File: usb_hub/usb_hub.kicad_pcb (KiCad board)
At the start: 2 copper layers, 100 x 23 mm, 127 parts, among them P1 CONN_01X02, U1 TPS2044B, U10 USB_A_FEMALE, U11 SN75240, U12 SN75240, U13 USB_A_FEMALE, U14 USB_A_FEMALE, U15 USB_A_FEMALE, U16 USB_A_FEMALE, U2 TPS2044B, U3 TUSB2077A, U4 TPS76333, U5 USB_A_MALE, U6 SN75240, U7 SN75240, U8 USB_A_FEMALE, U9 USB_A_FEMALE, X1 6 MHz

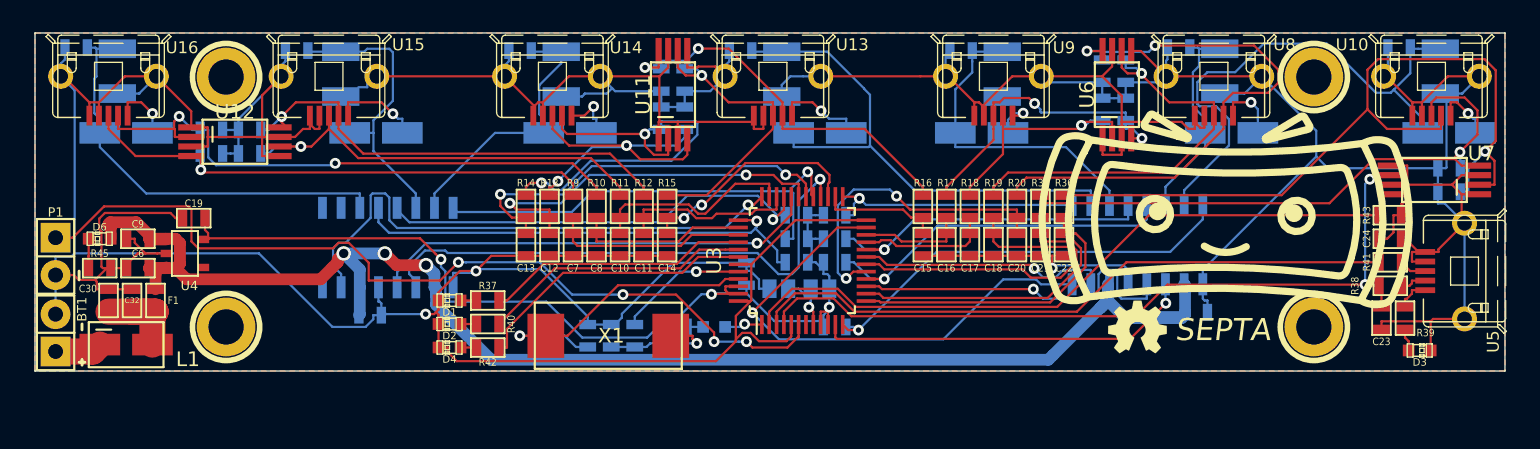
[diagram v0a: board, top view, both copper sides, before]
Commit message: started design for pick and place
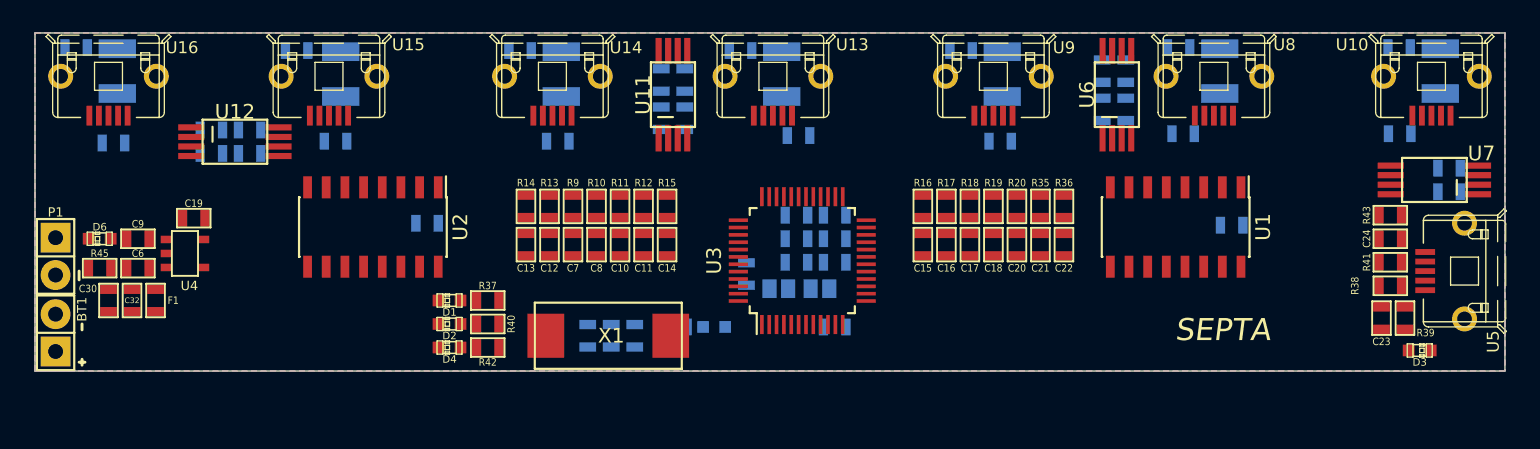
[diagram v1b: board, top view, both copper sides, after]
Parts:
- removed 1PIN, 2PIN, 3PIN, 4PIN: P***, Connect:1pin
- removed G***: LOGO, usb_hub:oshw
- removed G***: LOGO, usb_hub:LOGO
- removed L8: FERRITE, usb_hub:FB-28F0121
- L1: footprint usb_hub:FB-28F0121 -> SMD_Packages:SMD-0603; moved to B.Cu
- L2, L3, L4, L5, L6, L7: footprint usb_hub:FB-28F0121 -> SMD_Packages:SMD-0603
- U1, U2: moved to F.Cu
- moved L1 61.0 mm to (200.7, 86.4)
- moved L4 44.3 mm to (186.9, 86.0)
- moved L7 17.9 mm to (140.3, 86.5)
- moved L5 17.8 mm to (170.6, 86.4)
- moved L6 16.0 mm to (155.4, 86.4)
- moved L2 13.7 mm to (213.1, 85.9)
- moved L3 11.4 mm to (227.8, 85.9)
- moved C2 7.35 mm to (161.7, 91.9)
- moved C1 6.40 mm to (216.4, 92.1)
- moved U1 2.86 mm to (212.6, 92.2), turned to 270 degrees
- moved U2 1.73 mm to (158.0, 92.2), turned to 270 degrees
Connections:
- C30 pad 1: Net-(C30-Pad1) -> Net-(BT1-Pad1)
- C32 pad 1: Net-(C30-Pad1) -> Net-(BT1-Pad1)
- F1 pad 1: Net-(C30-Pad1) -> Net-(BT1-Pad1)
- L1 pad 1: Net-(BT1-Pad1) -> OUT3
- L1 pad 2: Net-(C30-Pad1) -> Net-(L1-Pad2)
- L2 pad 1: OUT3 -> OUT2
- L3 pad 1: OUT2 -> OUT1
- L4 pad 1: OUT1 -> OUT4
- L5 pad 1: OUT4 -> OUT5
- L6 pad 1: OUT5 -> OUT6
- L7 pad 1: OUT6 -> OUT7
- U10 pad 1: Net-(L4-Pad2) -> Net-(L3-Pad2)
- U13 pad 1: Net-(L5-Pad2) -> Net-(L4-Pad2)
- U14 pad 1: Net-(L6-Pad2) -> Net-(L5-Pad2)
- U15 pad 1: Net-(L7-Pad2) -> Net-(L6-Pad2)
- U16 pad 1: Net-(L8-Pad2) -> Net-(L7-Pad2)
- U8 pad 1: Net-(L3-Pad2) -> Net-(L2-Pad2)
- U9 pad 1: Net-(L2-Pad2) -> Net-(L1-Pad2)
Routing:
- net GND: track 460.0 -> 0.00 mm, vias 3 -> 0
- net VCC: track 120.9 -> 0.00 mm, vias 3 -> 0
- net 3.3V: track 68.3 -> 0.00 mm, vias 3 -> 0
- net RST: track 60.3 -> 0.00 mm, vias 4 -> 0
- net DM1: track 54.8 -> 0.00 mm, vias 1 -> 0
- net DM0: track 53.6 -> 0.00 mm, vias 2 -> 0
- net DP0: track 51.5 -> 0.00 mm
- net DP0PUR: track 46.1 -> 0.00 mm
- net DP1: track 41.3 -> 0.00 mm, vias 1 -> 0
- net DM7: track 39.6 -> 0.00 mm, vias 2 -> 0
- net DM2: track 38.7 -> 0.00 mm, vias 2 -> 0
- net PWRON7: track 37.3 -> 0.00 mm, vias 1 -> 0
- net PWRON5: track 37.2 -> 0.00 mm, vias 1 -> 0
- net DP7: track 36.5 -> 0.00 mm, vias 1 -> 0
- net OUT4: track 36.2 -> 0.00 mm
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
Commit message: finished routing. need to check bom and trace widths and pos file
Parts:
- removed C32: 4.7uF, SMD_Packages:SMD-0603
- removed C33, C34, C35, C36: 100uF, SMD_Packages:SMD-1210
- removed C37, C38, C39, C40: .1uF, SMD_Packages:SMD-0603
- removed F1: FUSE, SMD_Packages:SMD-0603
- removed JP1, JP2: JUMPER, Connect:GS2
- C18: value 22pF -> 10uF; footprint SMD_Packages:SMD-0603 -> SMD_Packages:SMD-1206
- C19: value 4.7uF -> 22pF
- C2, C25, C26, C29, C3, L1, L2, L3, L4, L5, L6, L7, R33, R34: moved to F.Cu
- C24: value 22pF -> 100uF; footprint SMD_Packages:SMD-0603 -> SMD_Packages:SMD-1210
- C27: value .1uF -> 10uF; footprint SMD_Packages:SMD-0603 -> SMD_Packages:SMD-1206; moved to F.Cu
- C28, C31: value .1uF -> 100uF; footprint SMD_Packages:SMD-0603 -> SMD_Packages:SMD-1210; moved to F.Cu
- C30: value .1uF -> 100uF; footprint SMD_Packages:SMD-0603 -> SMD_Packages:SMD-1210
- C6: value 4.7uF -> 1uF
- C9: value .1uF -> 22pF
- D1, D2, D4, D6: value LED(G) -> LED
- R10, R11, R12, R13, R14, R15, R16, R17, R18, R19, R20, R35, R36, R38, R41, R9: value 27 -> 30
- R37, R39, R40, R42, R44, R45: value 510 -> 1k
- U10, U13, U14, U15, U16, U8, U9: value USB_A_FEMALE -> USB_MICRO_OUT; footprint ab2_usb:AB2_USB_MICRO_SMD -> apro_lib:MICRO_USB
- U11, U12, U6, U7: footprint usb_hub:TSSOP8 -> Housings_SSOP:TSSOP-8_4.4x3mm_Pitch0.65mm
- U5: footprint ab2_usb:AB2_USB_MICRO_SMD -> apro_lib:MICRO_USB
- moved C31 90.8 mm to (137.3, 87.5), turned to 270 degrees
- moved C27 76.0 mm to (139.2, 98.8), turned to 90 degrees
- moved C29 66.2 mm to (164.6, 86.6), turned to 0 degrees
- moved C19 58.3 mm to (204.1, 93.5), turned to 270 degrees
- moved C18 52.9 mm to (147.3, 96.0), turned to 180 degrees
- moved C26 31.6 mm to (231.6, 88.8), turned to 180 degrees
- moved C9 27.9 mm to (169.9, 93.5), turned to 270 degrees
- moved C30 26.2 mm to (161.4, 82.2), turned to 270 degrees
- moved C22 19.7 mm to (224.5, 96.3), turned to 180 degrees
- moved C14 18.5 mm to (196.5, 93.5)
- moved C24 12.1 mm to (222.0, 82.0), turned to 270 degrees
- moved C25 8.98 mm to (206.6, 81.3), turned to 180 degrees
- moved C13 8.89 mm to (177.3, 93.5)
- moved R14 7.24 mm to (175.6, 90.8)
- moved U7 7.13 mm to (223.3, 90.7), turned to 270 degrees
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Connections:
- BT1 pad 1: Net-(BT1-Pad1) -> VCC
- C18 pad 1: Net-(C18-Pad1) -> 3.3V
- C19 pad 1: 3.3V -> Net-(C19-Pad1)
- C22 pad 1: Net-(C22-Pad1) -> DM0
- C23 pad 1: DM0 -> DP0
- C24 pad 1: DP0 -> GND
- C24 pad 2: GND -> OUT2
- C25 pad 2: OUT2 -> OUT3
- C26 pad 2: OUT3 -> OUT1
- C27 pad 1: GND -> VCC
- C27 pad 2: OUT2 -> GND
- C28 pad 2: OUT3 -> OUT4
- C29 pad 2: OUT1 -> OUT5
- C30 pad 1: Net-(BT1-Pad1) -> GND
- C30 pad 2: GND -> OUT6
- C31 pad 2: OUT1 -> OUT7
- C9 pad 1: VCC -> Net-(C9-Pad1)
- R11 pad 1: Net-(C10-Pad1) -> Net-(C9-Pad1)
- R12 pad 1: Net-(C11-Pad1) -> Net-(C10-Pad1)
- R13 pad 1: Net-(C12-Pad1) -> Net-(C11-Pad1)
- R14 pad 1: Net-(C13-Pad1) -> Net-(C12-Pad1)
- R15 pad 1: Net-(C14-Pad1) -> Net-(C13-Pad1)
- R16 pad 1: Net-(C15-Pad1) -> Net-(C14-Pad1)
- R17 pad 1: Net-(C16-Pad1) -> Net-(C15-Pad1)
- R18 pad 1: Net-(C17-Pad1) -> Net-(C16-Pad1)
- R19 pad 1: Net-(C18-Pad1) -> Net-(C17-Pad1)
- R20 pad 1: Net-(C20-Pad1) -> Net-(C19-Pad1)
- R35 pad 1: Net-(C21-Pad1) -> Net-(C20-Pad1)
- R36 pad 1: Net-(C22-Pad1) -> Net-(C21-Pad1)
- R38 pad 1: Net-(R38-Pad1) -> DM0
- R38 pad 2: DM0 -> Net-(R38-Pad2)
- R41 pad 1: Net-(R41-Pad1) -> DP0
- R41 pad 2: DP0 -> Net-(R41-Pad2)
- R43 pad 1: DP0 -> DP0PUR
- R43 pad 2: DP0PUR -> DP0
- U3 pad 13: Net-(C22-Pad1) -> Net-(C21-Pad1)
- U3 pad 14: Net-(C21-Pad1) -> Net-(C20-Pad1)
- U3 pad 17: Net-(C20-Pad1) -> Net-(C19-Pad1)
- U3 pad 18: Net-(C18-Pad1) -> Net-(C17-Pad1)
- U3 pad 21: Net-(C17-Pad1) -> Net-(C16-Pad1)
- U3 pad 22: Net-(C16-Pad1) -> Net-(C15-Pad1)
- U3 pad 26: Net-(C15-Pad1) -> Net-(C14-Pad1)
- U3 pad 27: Net-(C14-Pad1) -> Net-(C13-Pad1)
- U3 pad 30: Net-(C13-Pad1) -> Net-(C12-Pad1)
- U3 pad 31: Net-(C12-Pad1) -> Net-(C11-Pad1)
- U3 pad 34: Net-(C11-Pad1) -> Net-(C10-Pad1)
- U3 pad 35: Net-(C10-Pad1) -> Net-(C9-Pad1)
- U3 pad 8: Net-(JP1-Pad2) -> 3.3V
- U5 pad 2: Net-(R38-Pad1) -> Net-(R38-Pad2)
- U5 pad 3: Net-(R41-Pad1) -> Net-(R41-Pad2)
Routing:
- net GND: track 0.00 -> 481.1 mm, vias 0 -> 6
- net VCC: track 0.00 -> 127.5 mm, vias 0 -> 3
- net RST: track 0.00 -> 71.2 mm, vias 0 -> 1
- net 3.3V: track 0.00 -> 64.3 mm, vias 0 -> 3
- net OC3: track 0.00 -> 63.3 mm, vias 0 -> 2
- net DP0: track 0.00 -> 62.1 mm
- net DM0: track 0.00 -> 48.9 mm
- net DP0PUR: track 0.00 -> 47.6 mm, vias 0 -> 2
- net OC7: track 0.00 -> 37.3 mm, vias 0 -> 2
- net OC5: track 0.00 -> 37.2 mm, vias 0 -> 2
- net PWRON5: track 0.00 -> 36.3 mm, vias 0 -> 2
- net DM7: track 0.00 -> 36.2 mm, vias 0 -> 2
- net DP7: track 0.00 -> 35.8 mm, vias 0 -> 2
- net PWRON1: track 0.00 -> 35.7 mm
- net PWRON7: track 0.00 -> 35.6 mm, vias 0 -> 2
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- added copper zone on B.Cu, net (none)
- added copper zone on F.Cu, net (none)
- removed copper zone on B.Cu, net GND
- removed copper zone on F.Cu, net GND
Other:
- net class Default: via_dia 0.7366 -> 0.6858; via_drill 0.381 -> 0.3302

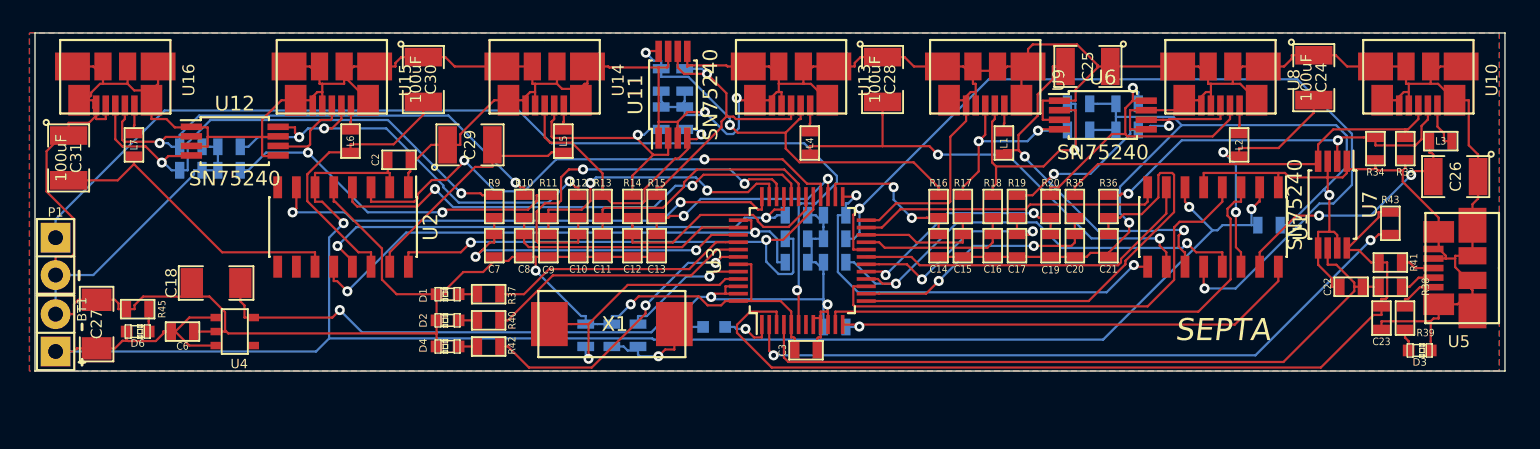
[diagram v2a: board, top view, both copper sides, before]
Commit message: usb_hub ready for review. Audio schematic in the works
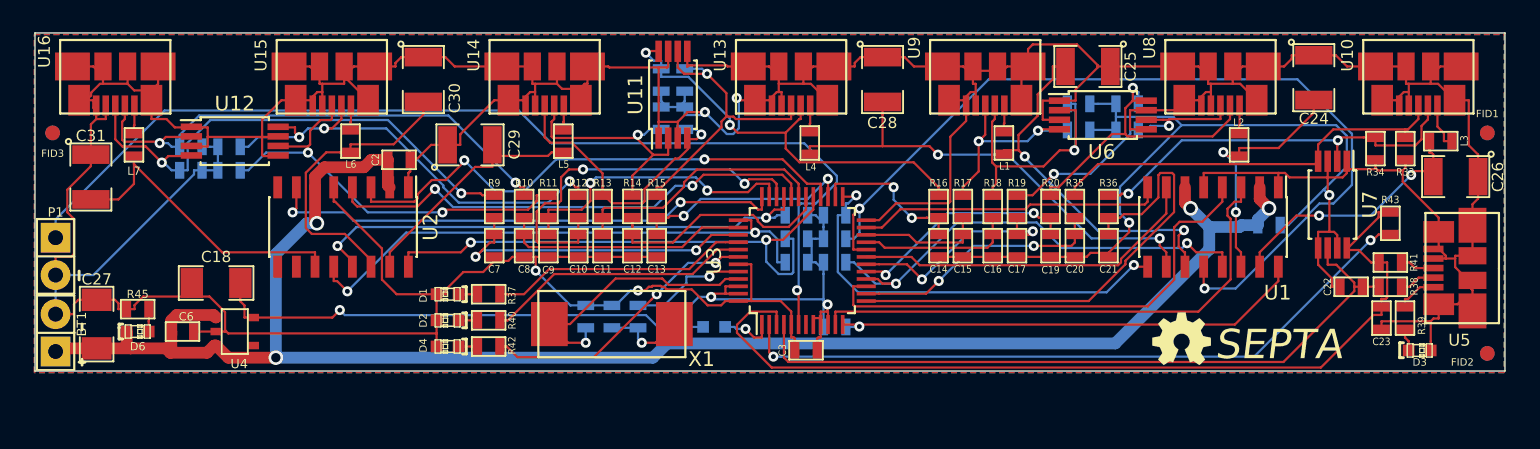
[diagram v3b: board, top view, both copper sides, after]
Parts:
- added FID1: VAL**, apro_lib:SBA_FID, F.Cu at (233.8, 85.8)
- added FID2: VAL**, apro_lib:SBA_FID, F.Cu at (233.8, 100.8)
- added FID3: VAL**, apro_lib:SBA_FID, F.Cu at (136.2, 85.8)
- added FID4: VAL**, apro_lib:SBA_FID, B.Cu at (233.8, 85.8)
- added FID5: VAL**, apro_lib:SBA_FID, B.Cu at (233.8, 100.8)
- added FID6: VAL**, apro_lib:SBA_FID, B.Cu at (136.2, 85.8)
- added G***: LOGO, usb_hub:oshw, F.Cu at (213.0, 99.8)
- moved C31 1.99 mm to (138.8, 88.8)
- moved C4 1.27 mm to (172.5, 98.3)
- moved C5 1.27 mm to (174.2, 98.3)
- moved R8 1.27 mm to (176.0, 98.3)
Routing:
- net VCC: track 127.5 -> 122.9 mm, vias 3 -> 4
- net GND: track 481.1 -> 477.3 mm
- net (no net): track 0.00 -> 3.07 mm
- net Net-(C5-Pad1): track 6.88 -> 5.64 mm
- net Net-(C4-Pad1): track 17.4 -> 18.5 mm
- net OUT6: track 19.3 -> 20.4 mm
- net PORTDIS: track 20.3 -> 19.3 mm
- net Net-(R8-Pad1): track 8.62 -> 8.05 mm
- added copper zone on B.Cu, net GND
- added copper zone on F.Cu, net GND
- removed copper zone on B.Cu, net (none)
- removed copper zone on F.Cu, net (none)

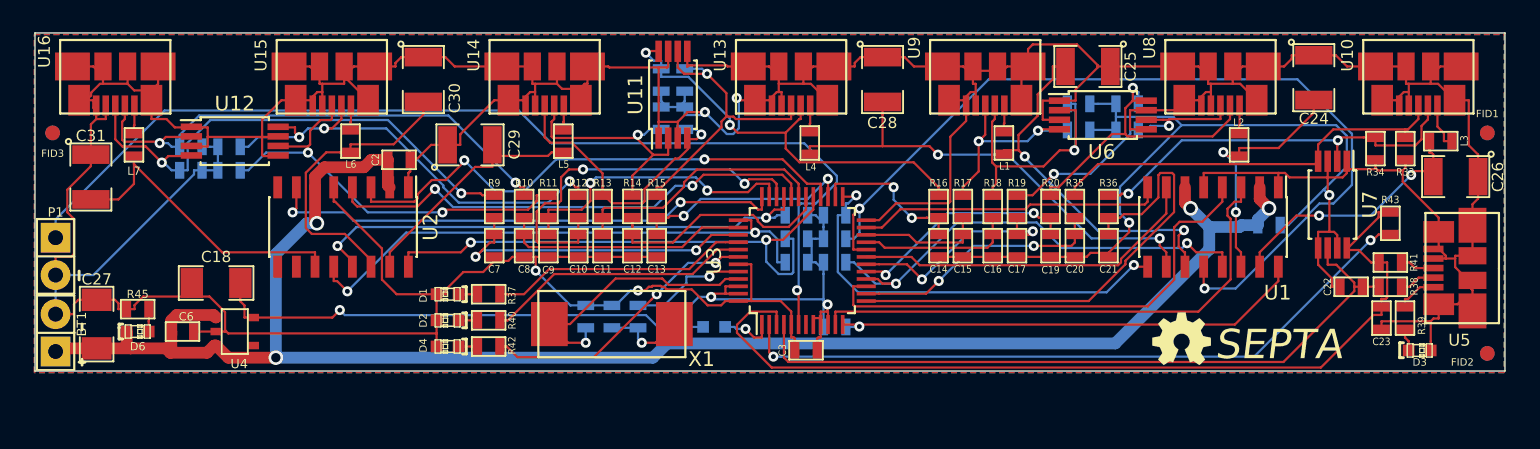
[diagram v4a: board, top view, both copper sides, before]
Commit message: placed all components on one side to make assembly easier. Ready for review
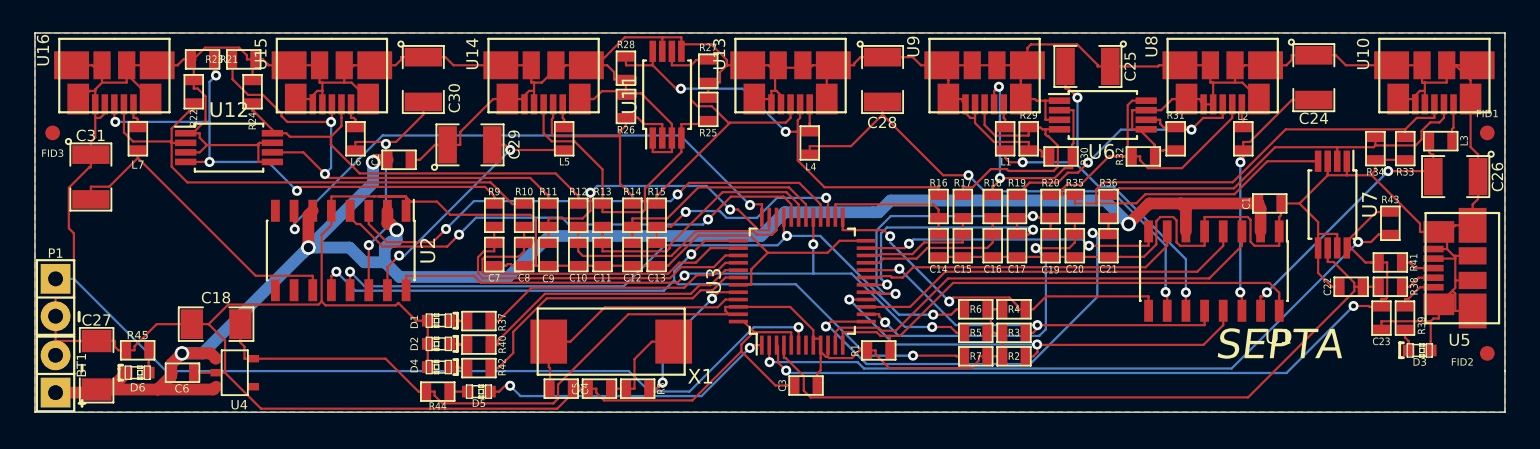
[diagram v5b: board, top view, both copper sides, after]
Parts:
- removed FID4, FID5, FID6: VAL**, apro_lib:SBA_FID
- removed G***: LOGO, usb_hub:oshw
- C1, C4, C5, D5, R1, R2, R21, R22, R23, R24, R25, R26, R27, R28, R29, R3, R30, R31, R32, R4, R44, R5, R6, R7, R8: moved to F.Cu
- moved R44 16.8 mm to (162.4, 103.4)
- moved D5 16.6 mm to (165.2, 103.4)
- moved R2 13.8 mm to (201.6, 101.0)
- moved R3 13.8 mm to (201.6, 99.4)
- moved R5 13.8 mm to (199.0, 99.4)
- moved R7 13.8 mm to (199.0, 101.0)
- moved R4 13.8 mm to (201.6, 97.8)
- moved R6 13.8 mm to (199.0, 97.8)
- moved R23 7.61 mm to (149.2, 80.8), turned to 180 degrees
- moved R21 7.58 mm to (146.4, 80.8), turned to 0 degrees
- moved C4 5.18 mm to (170.8, 103.2), turned to 0 degrees
- moved C5 4.97 mm to (173.4, 103.2), turned to 180 degrees
- moved R8 4.90 mm to (176.0, 103.2), turned to 180 degrees
- moved R24 4.07 mm to (149.8, 83.0), turned to 270 degrees
- moved R30 3.77 mm to (204.8, 87.4), turned to 0 degrees
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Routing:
- net OC3: track 63.3 -> 26.8 mm
- net DP1: track 28.0 -> 45.7 mm
- net SPND: track 3.67 -> 20.4 mm, vias 1 -> 2
- net OC7: track 37.3 -> 53.0 mm, vias 2 -> 3
- net RST: track 71.2 -> 56.8 mm
- net OC6: track 35.5 -> 48.6 mm, vias 2 -> 3
- net GND: track 477.3 -> 487.3 mm, vias 6 -> 0
- net Net-(C10-Pad1): track 26.5 -> 17.1 mm, vias 2 -> 0
- net 3.3V: track 64.0 -> 72.8 mm, vias 3 -> 0
- net OC5: track 37.2 -> 44.9 mm, vias 2 -> 3
- net DP0: track 62.1 -> 55.2 mm, vias 0 -> 2
- net Net-(C8-Pad1): track 16.9 -> 23.8 mm
- net PWRON2: track 33.3 -> 27.0 mm
- net Net-(C20-Pad1): track 17.3 -> 23.4 mm
- net Net-(C19-Pad1): track 15.6 -> 20.8 mm
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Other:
- board size 100 x 23 mm -> 100 x 25.8 mm

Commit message: cleaned up the usb hub project. waiting quote on elecrow
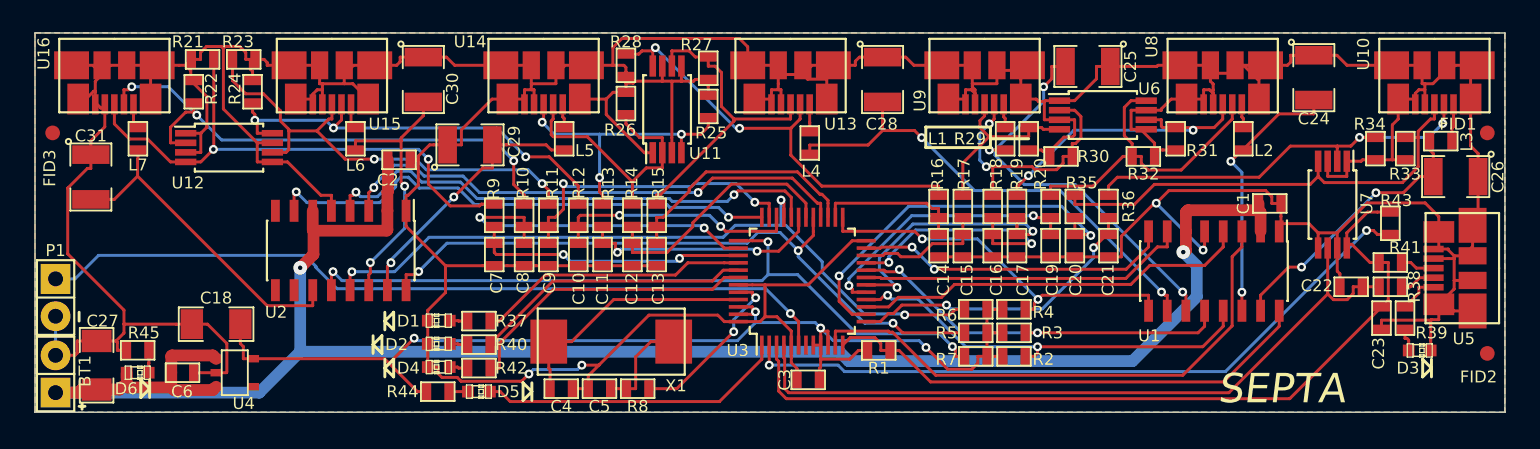
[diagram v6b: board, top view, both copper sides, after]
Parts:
- moved U11 1.00 mm to (178.0, 84.2)
- moved C3 0.41 mm to (187.6, 102.6)
- moved R25 0.20 mm to (180.8, 84.0)
- moved R26 0.20 mm to (175.2, 83.8)
- moved R28 0.20 mm to (175.2, 81.2)
- moved R27 0.20 mm to (180.8, 81.4)
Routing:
- net GND: track 487.3 -> 458.8 mm, vias 0 -> 4
- net DP1: track 45.7 -> 32.2 mm
- net VCC: track 120.3 -> 131.8 mm, vias 5 -> 2
- net Net-(C21-Pad1): track 31.1 -> 20.7 mm
- net Net-(C16-Pad1): track 10.9 -> 17.2 mm, vias 0 -> 2
- net 3.3V: track 72.8 -> 78.7 mm, vias 0 -> 4
- net DP3: track 18.0 -> 12.8 mm
- net PWRON1: track 32.1 -> 37.3 mm
- net Net-(C7-Pad1): track 22.6 -> 18.8 mm, vias 0 -> 2
- net PWRON7: track 38.8 -> 35.4 mm
- net DP0: track 55.2 -> 58.1 mm, vias 2 -> 0
- net Net-(C20-Pad1): track 23.4 -> 26.1 mm
- net DP6: track 34.9 -> 32.3 mm
- net Net-(C19-Pad1): track 20.8 -> 18.7 mm
- net RST: track 56.8 -> 54.7 mm
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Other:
- net class 4PCB removed
- net class Default: trace_width 0.1524 -> 0.2032; via_dia 0.6858 -> 0.6048; via_drill 0.3302 -> 0.3
- net class POWER removed
- rule pad_to_mask_clearance: 0.0508 -> 0
- rule trace_min: 0.1524 -> 0.2032
- rule via_min_drill: 0.3302 -> 0.3
- rule via_min_size: 0.3302 -> 0.3
